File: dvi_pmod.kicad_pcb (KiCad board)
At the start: 2 copper layers, 25 x 18.5 mm, 12 parts, among them J1 02x06, J2 Conn_01x02, J3 HDMI_A

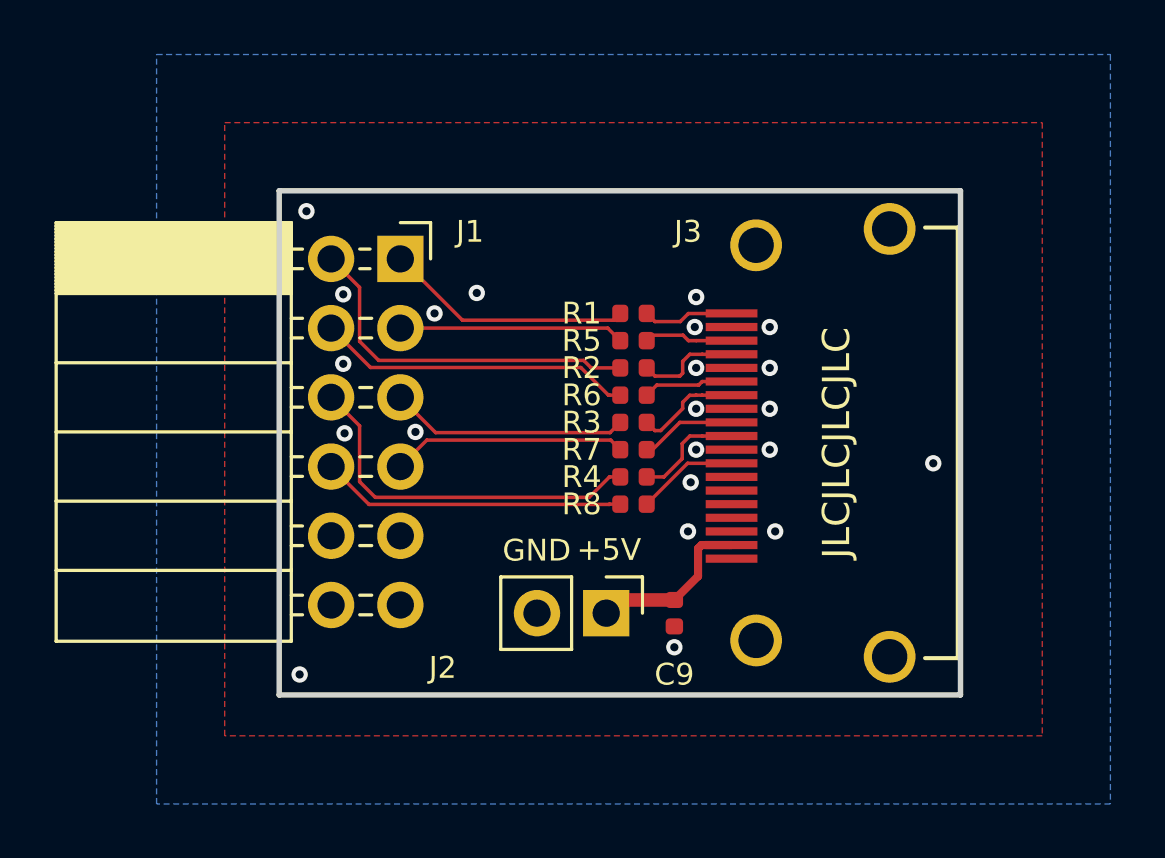
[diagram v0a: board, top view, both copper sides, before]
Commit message: New pinout and new layout
Signed-off-by: Sylvain Munaut <tnt@246tNt.com>
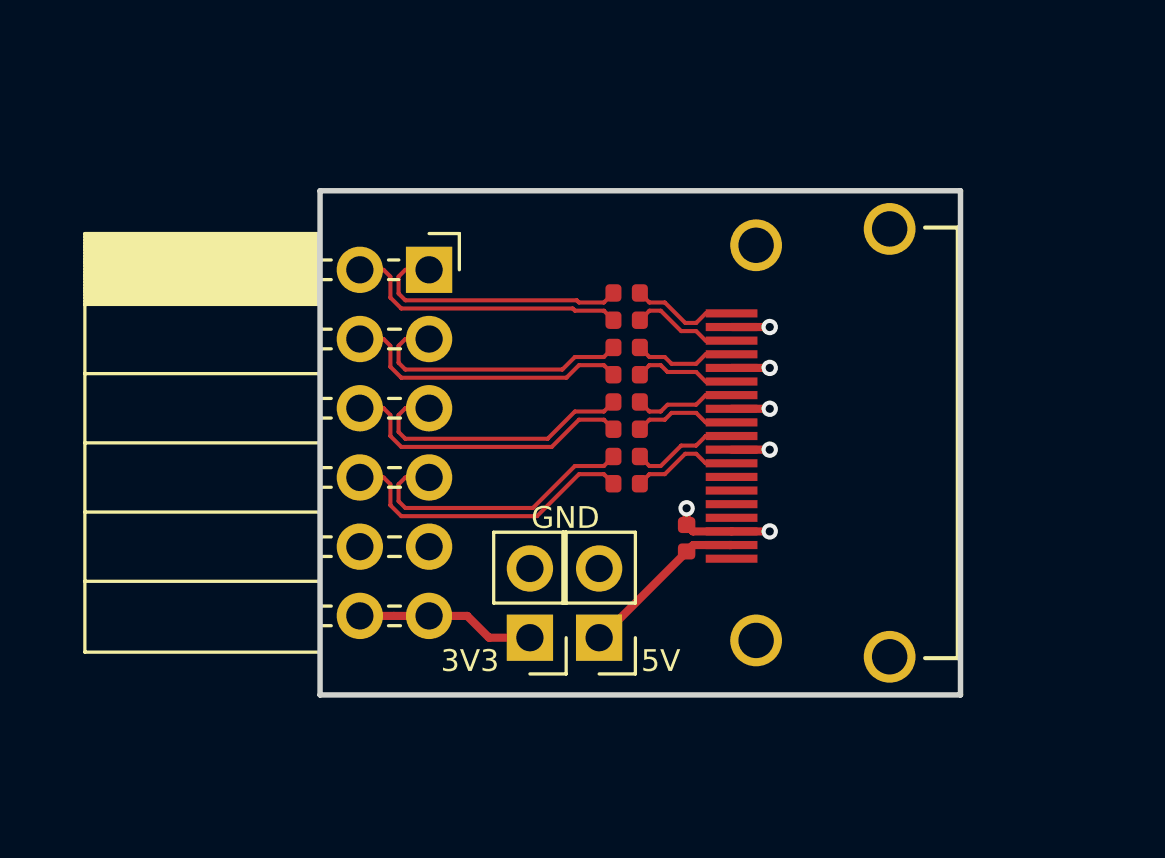
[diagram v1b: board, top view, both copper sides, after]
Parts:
- added J1: Conn_01x02, Connector_PinHeader_2.54mm:PinHeader_1x02_P2.54mm_Vertical, F.Cu at (136.2, 83.9)
- J4: renamed from J3; value HDMI_A -> NOT_HDMI_A
- moved C1 2.79 mm to (141.9, 80.2), turned to 270 degrees
- moved J2 1.13 mm to (132.5, 70.4)
- moved J3 0.94 mm to (138.7, 83.9), turned to 180 degrees
- moved R1 0.79 mm to (139.8, 71.2)
- moved R2 0.79 mm to (139.8, 73.2)
- moved R3 0.79 mm to (139.8, 75.2)
- moved R4 0.79 mm to (139.8, 77.2)
- moved R5 0.79 mm to (139.8, 72.2)
- moved R6 0.79 mm to (139.8, 74.2)
- moved R7 0.79 mm to (139.8, 76.2)
- moved R8 0.79 mm to (139.8, 78.2)
- renumbered C9 to C1, J1 to J2, J2 to J3
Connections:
- J2 pad 11: Net-(J1-Pad11) -> +3V3
- J2 pad 12: Net-(J1-Pad12) -> +3V3
- J2 pad 2: /PMOD_D1+ -> /PMOD_D2-
- J2 pad 3: /PMOD_D2- -> /PMOD_D1+
- J2 pad 6: /PMOD_CK+ -> /PMOD_D0-
- J2 pad 7: /PMOD_D0- -> /PMOD_CK+
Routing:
- net GND: track 0.00 -> 9.36 mm, vias 22 -> 6
- net +3V3: track 0.00 -> 6.57 mm
- net /PMOD_D1+: track 13.4 -> 10.2 mm
- net /PMOD_CK+: track 13.6 -> 10.6 mm
- net /PMOD_D0-: track 8.62 -> 10.9 mm
- net /PMOD_D2-: track 8.26 -> 10.5 mm
- net /PMOD_D0+: track 8.76 -> 10.4 mm
- net /PMOD_D1-: track 11.6 -> 10.7 mm
- net /PMOD_D2+: track 9.11 -> 10.0 mm
- net /D2-: track 3.28 -> 3.97 mm
- net /D2+: track 3.36 -> 3.97 mm
- removed copper zone on F.Cu, net GND
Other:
- board size 25 x 18.5 mm -> 23.5 x 18.5 mm
- net class Default: clearance 0.13 -> 0.15; trace_width 0.13 -> 0.15
- rule trace_clearance: 0.13 -> 0.15
- board text added: "3V3"
- board text added: "5V"
- board text removed: "+5V"
- board text removed: "JLCJLCJLCJLC"
